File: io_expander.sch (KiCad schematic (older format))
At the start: 11 parts, among them IC1 MCP23008, P6 CONN_01X16, Q1 MTM232270LBF, Q2 MTM232270LBF, Q3 MTM232270LBF, Q4 MTM232270LBF, Q5 MTM232270LBF, Q6 MTM232270LBF, Q7 MTM232270LBF, Q8 MTM232270LBF

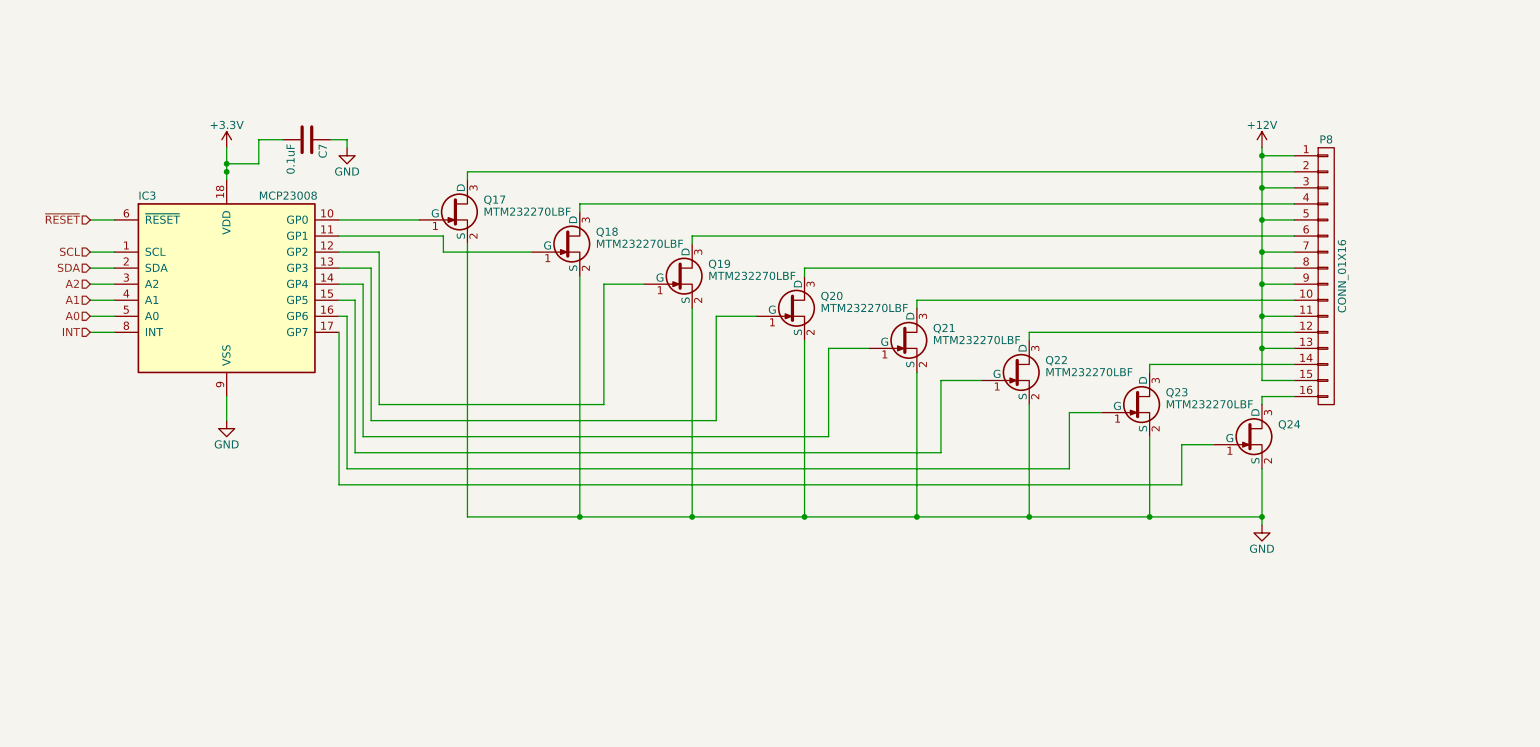
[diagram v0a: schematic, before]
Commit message: Rev B, Added Flywheel Diodes
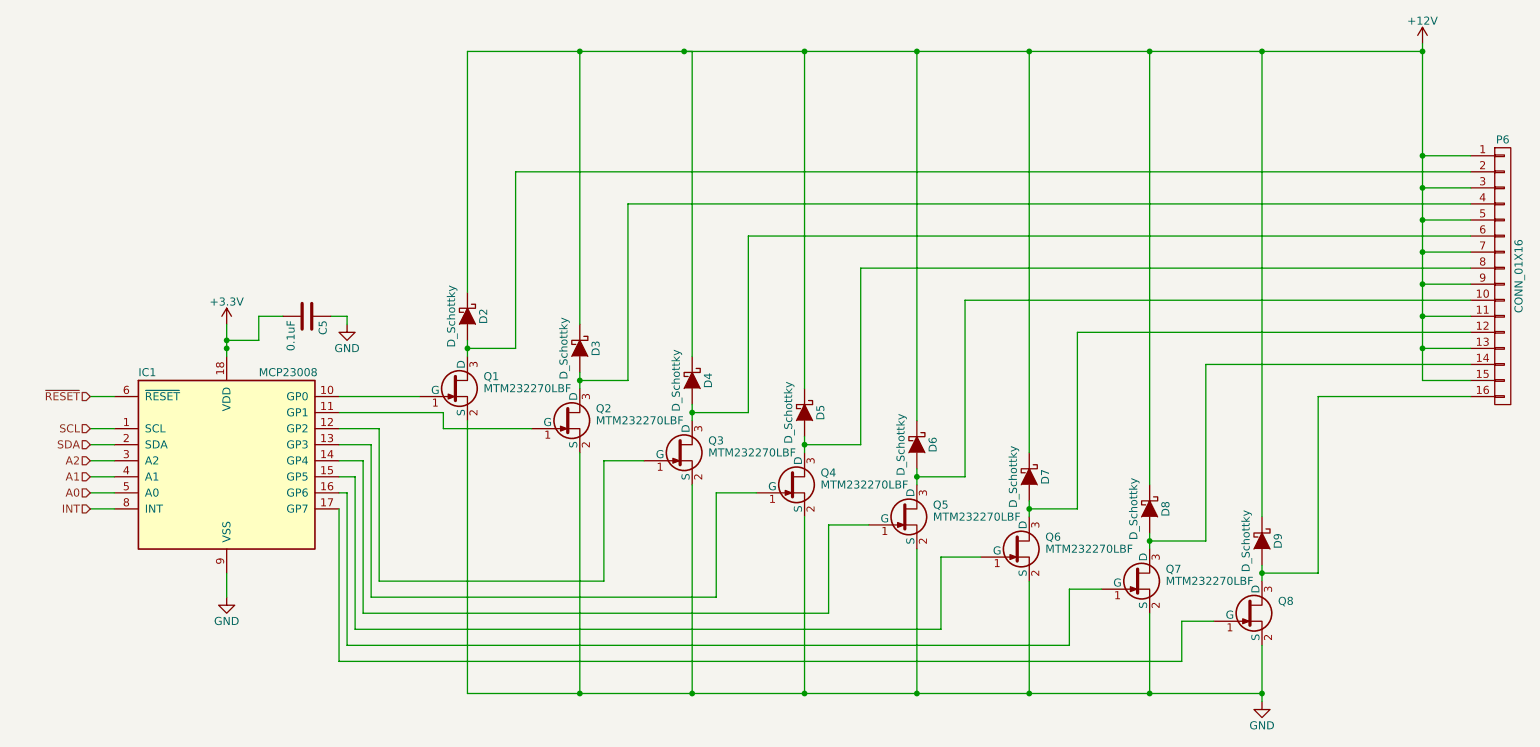
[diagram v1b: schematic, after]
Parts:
- added D17, D2, D3, D4, D5, D6, D7, D8: D_Schottky, Project Folder:microSMP, symbol D_Schottky
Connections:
- net +12V: now also D17.1 (K), D2.1 (K), D3.1 (K), D4.1 (K), D5.1 (K), D6.1 (K), D7.1 (K), D8.1 (K)
- net at P6.10 (P10), Q5.3 (D): now also D6.2 (A)
- net at P6.12 (P12), Q6.3 (D): now also D7.2 (A)
- net at P6.14 (P14), Q7.3 (D): now also D8.2 (A)
- net at P6.16 (P16), Q8.3 (D): now also D17.2 (A)
- net at P6.2 (P2), Q1.3 (D): now also D2.2 (A)
- net at P6.4 (P4), Q2.3 (D): now also D3.2 (A)
- net at P6.6 (P6), Q3.3 (D): now also D4.2 (A)
- net at P6.8 (P8), Q4.3 (D): now also D5.2 (A)
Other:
- moved on the sheet: C5, IC1, P6, Q1, Q2, Q3, Q4, Q5, Q6, Q7, Q8

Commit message: Added Fiducials and Fixed Diode Orientation
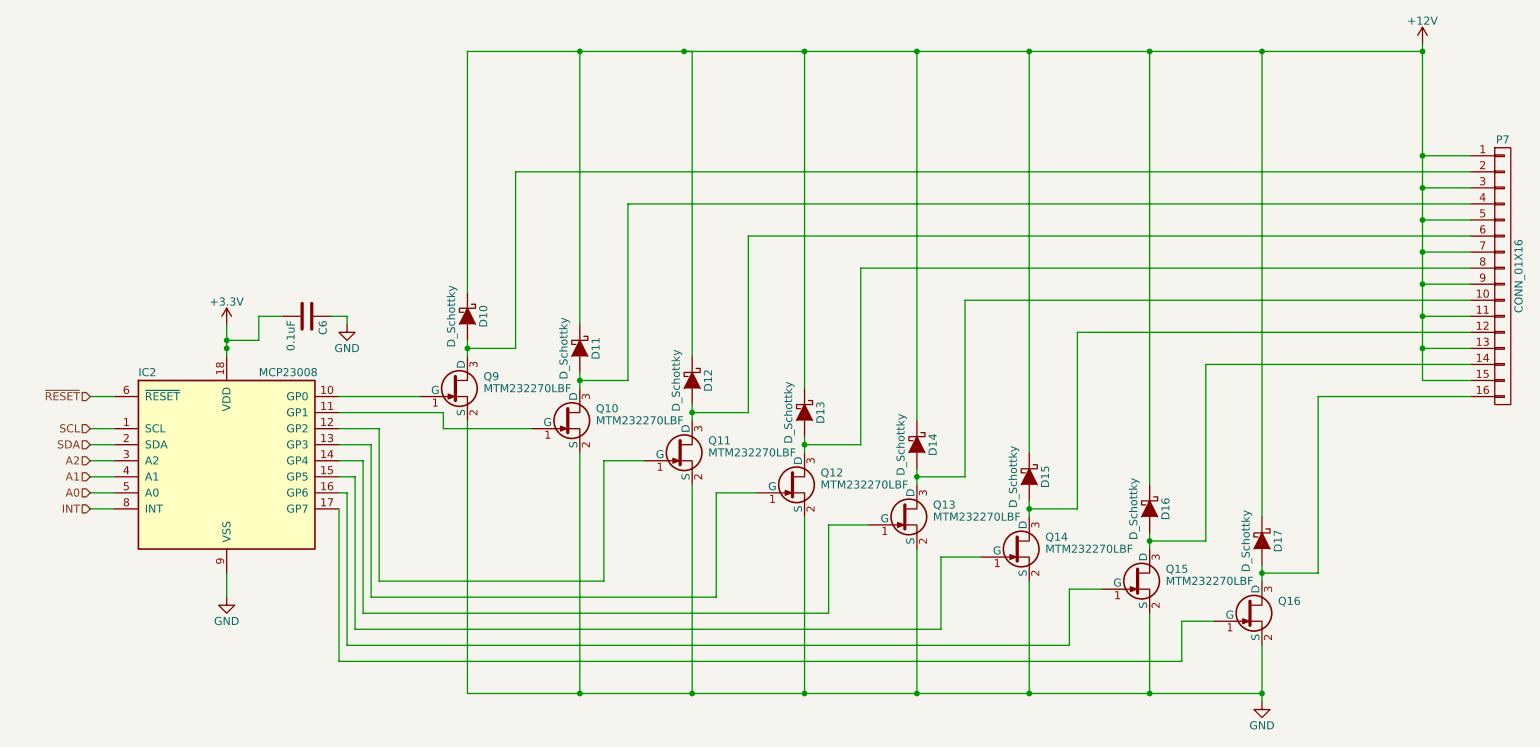
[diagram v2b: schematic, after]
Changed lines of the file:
@@
 $Descr A4 11693 8268
 encoding utf-8
-Sheet 2 5
+Sheet 3 5
 Title "The Open Bar Control Board"
-Date "2017-01-17"
-Rev "B"
+Date "2017-03-21"
+Rev "C"
 Comp "The Open Bar"
 Comment1 ""
@@
 AR Path="/56D78A1E/56D75806" Ref="P8"  Part="1"
 AR Path="/56D79252/56D75806" Ref="P9"  Part="1"
-F 0 "P6" H 11000 4400 50  0000 C CNN
+F 0 "P7" H 11000 4400 50  0000 C CNN
 F 1 "CONN_01X16" V 11100 3550 50  0000 C CNN
 F 2 "Terminal_Blocks:TerminalBlock_Pheonix_PT-3.5mm_16pol" H 11000 3550 50  0001 C CNN
@@
 AR Path="/56D78A1E/56D75807" Ref="Q17"  Part="1"
 AR Path="/56D79252/56D75807" Ref="Q25"  Part="1"
-F 0 "Q1" H 4650 4325 50  0000 L CNN
+F 0 "Q9" H 4650 4325 50  0000 L CNN
 F 1 "MTM232270LBF" H 4650 4250 50  0000 L CNN
 F 2 "TO_SOT_Packages_SMD:SC-70" H 4650 4175 50  0001 L CIN
@@
 AR Path="/56D78A1E/56D75808" Ref="Q18"  Part="1"
 AR Path="/56D79252/56D75808" Ref="Q26"  Part="1"
-F 0 "Q2" H 5350 4525 50  0000 L CNN
+F 0 "Q10" H 5350 4525 50  0000 L CNN
 F 1 "MTM232270LBF" H 5350 4450 50  0000 L CNN
 F 2 "TO_SOT_Packages_SMD:SC-70" H 5350 4375 50  0001 L CIN
@@
 AR Path="/56D78A1E/56D75809" Ref="Q19"  Part="1"
 AR Path="/56D79252/56D75809" Ref="Q27"  Part="1"
-F 0 "Q3" H 6050 4725 50  0000 L CNN
+F 0 "Q11" H 6050 4725 50  0000 L CNN
 F 1 "MTM232270LBF" H 6050 4650 50  0000 L CNN
 F 2 "TO_SOT_Packages_SMD:SC-70" H 6050 4575 50  0001 L CIN
@@
 AR Path="/56D78A1E/56D7580A" Ref="Q20"  Part="1"
 AR Path="/56D79252/56D7580A" Ref="Q28"  Part="1"
-F 0 "Q4" H 6750 4925 50  0000 L CNN
+F 0 "Q12" H 6750 4925 50  0000 L CNN
 F 1 "MTM232270LBF" H 6750 4850 50  0000 L CNN
 F 2 "TO_SOT_Packages_SMD:SC-70" H 6750 4775 50  0001 L CIN
@@
 AR Path="/56D78A1E/56D7580B" Ref="Q21"  Part="1"
 AR Path="/56D79252/56D7580B" Ref="Q29"  Part="1"
-F 0 "Q5" H 7450 5125 50  0000 L CNN
+F 0 "Q13" H 7450 5125 50  0000 L CNN
 F 1 "MTM232270LBF" H 7450 5050 50  0000 L CNN
 F 2 "TO_SOT_Packages_SMD:SC-70" H 7450 4975 50  0001 L CIN
@@
 AR Path="/56D78A1E/56D7580C" Ref="Q22"  Part="1"
 AR Path="/56D79252/56D7580C" Ref="Q30"  Part="1"
-F 0 "Q6" H 8150 5325 50  0000 L CNN
+F 0 "Q14" H 8150 5325 50  0000 L CNN
 F 1 "MTM232270LBF" H 8150 5250 50  0000 L CNN
 F 2 "TO_SOT_Packages_SMD:SC-70" H 8150 5175 50  0001 L CIN
@@
 AR Path="/56D78A1E/56D7580D" Ref="Q23"  Part="1"
 AR Path="/56D79252/56D7580D" Ref="Q31"  Part="1"
-F 0 "Q7" H 8900 5525 50  0000 L CNN
+F 0 "Q15" H 8900 5525 50  0000 L CNN
 F 1 "MTM232270LBF" H 8900 5450 50  0000 L CNN
 F 2 "TO_SOT_Packages_SMD:SC-70" H 8900 5375 50  0001 L CIN
@@
 AR Path="/56D78A1E/56D7580E" Ref="Q24"  Part="1"
 AR Path="/56D79252/56D7580E" Ref="Q32"  Part="1"
-F 0 "Q8" H 9600 5725 50  0000 L CNN
+F 0 "Q16" H 9600 5725 50  0000 L CNN
 F 1 "MTM232270LBF" H 9600 5650 50  0001 L CNN
 F 2 "TO_SOT_Packages_SMD:SC-70" H 9600 5575 50  0001 L CIN
@@
 AR Path="/56D78A1E/56D7580F" Ref="#PWR034"  Part="1"
 AR Path="/56D79252/56D7580F" Ref="#PWR039"  Part="1"
-F 0 "#PWR039" H 10500 1950 50  0001 C CNN
+F 0 "#PWR029" H 10500 1950 50  0001 C CNN
 F 1 "+12V" H 10500 2240 50  0000 C CNN
 F 2 "" H 10500 2100 50  0000 C CNN
@@
 AR Path="/56D78A1E/56D75818" Ref="#PWR035"  Part="1"
 AR Path="/56D79252/56D75818" Ref="#PWR040"  Part="1"
-F 0 "#PWR040" H 9500 5950 50  0001 C CNN
+F 0 "#PWR030" H 9500 5950 50  0001 C CNN
 F 1 "GND" H 9500 6050 50  0000 C CNN
 F 2 "" H 9500 6200 50  0000 C CNN
@@
 AR Path="/56D78A1E/56D75820" Ref="IC3"  Part="1"
 AR Path="/56D79252/56D75820" Ref="IC4"  Part="1"
-F 0 "IC1" H 2500 5250 50  0000 L CNN
+F 0 "IC2" H 2500 5250 50  0000 L CNN
 F 1 "MCP23008" H 3250 5250 50  0000 L CNN
 F 2 "Housings_SOIC:SOIC-18_7.5x11.6mm_Pitch1.27mm" H 3050 4700 50  0001 C CIN
@@
 AR Path="/56D78A1E/56D75821" Ref="#PWR036"  Part="1"
 AR Path="/56D79252/56D75821" Ref="#PWR041"  Part="1"
-F 0 "#PWR041" H 3050 5300 50  0001 C CNN
+F 0 "#PWR031" H 3050 5300 50  0001 C CNN
 F 1 "GND" H 3050 5400 50  0000 C CNN
 F 2 "" H 3050 5550 50  0000 C CNN
@@
 AR Path="/56D78A1E/56D75822" Ref="#PWR037"  Part="1"
 AR Path="/56D79252/56D75822" Ref="#PWR042"  Part="1"
-F 0 "#PWR042" H 3050 3700 50  0001 C CNN
+F 0 "#PWR032" H 3050 3700 50  0001 C CNN
 F 1 "+3.3V" H 3050 3990 50  0000 C CNN
 F 2 "" H 3050 3850 50  0000 C CNN
@@
 AR Path="/56D78A1E/56D75826" Ref="C7"  Part="1"
 AR Path="/56D79252/56D75826" Ref="C8"  Part="1"
-F 0 "C5" H 3575 3900 50  0000 L CNN
+F 0 "C6" H 3575 3900 50  0000 L CNN
 F 1 "0.1uF" H 3575 3700 50  0000 L CNN
 F 2 "Capacitors_SMD:C_0402" H 3588 3650 50  0001 C CNN
@@
 AR Path="/56D78A1E/56D75827" Ref="#PWR038"  Part="1"
 AR Path="/56D79252/56D75827" Ref="#PWR043"  Part="1"
-F 0 "#PWR043" H 3800 3600 50  0001 C CNN
+F 0 "#PWR033" H 3800 3600 50  0001 C CNN
 F 1 "GND" H 3800 3700 50  0000 C CNN
 F 2 "" H 3800 3850 50  0000 C CNN
@@
 AR Path="/56D78A1E/587E8B5C" Ref="D18"  Part="1"
 AR Path="/56D79252/587E8B5C" Ref="D26"  Part="1"
-F 0 "D2" H 4550 3900 50  0000 C CNN
+F 0 "D10" H 4550 3900 50  0000 C CNN
 F 1 "D_Schottky" H 4550 3700 50  0000 C CNN
 F 2 "Project Folder:microSMP" H 4550 3800 50  0001 C CNN
@@
 AR Path="/56D78A1E/587E90C4" Ref="D19"  Part="1"
 AR Path="/56D79252/587E90C4" Ref="D27"  Part="1"
-F 0 "D3" H 5250 4100 50  0000 C CNN
+F 0 "D11" H 5250 4100 50  0000 C CNN
 F 1 "D_Schottky" H 5250 3900 50  0000 C CNN
 F 2 "Project Folder:microSMP" H 5250 4000 50  0001 C CNN
@@
 AR Path="/56D78A1E/587E9153" Ref="D20"  Part="1"
 AR Path="/56D79252/587E9153" Ref="D28"  Part="1"
-F 0 "D4" H 5950 4300 50  0000 C CNN
+F 0 "D12" H 5950 4300 50  0000 C CNN
 F 1 "D_Schottky" H 5950 4100 50  0000 C CNN
 F 2 "Project Folder:microSMP" H 5950 4200 50  0001 C CNN
@@
 AR Path="/56D78A1E/587E91AD" Ref="D21"  Part="1"
 AR Path="/56D79252/587E91AD" Ref="D29"  Part="1"
-F 0 "D5" H 6650 4500 50  0000 C CNN
+F 0 "D13" H 6650 4500 50  0000 C CNN
 F 1 "D_Schottky" H 6650 4300 50  0000 C CNN
 F 2 "Project Folder:microSMP" H 6650 4400 50  0001 C CNN
@@
 AR Path="/56D78A1E/587E920E" Ref="D22"  Part="1"
 AR Path="/56D79252/587E920E" Ref="D30"  Part="1"
-F 0 "D6" H 7350 4700 50  0000 C CNN
+F 0 "D14" H 7350 4700 50  0000 C CNN
 F 1 "D_Schottky" H 7350 4500 50  0000 C CNN
 F 2 "Project Folder:microSMP" H 7350 4600 50  0001 C CNN
@@
 AR Path="/56D78A1E/587E926C" Ref="D23"  Part="1"
 AR Path="/56D79252/587E926C" Ref="D31"  Part="1"
-F 0 "D7" H 8050 4900 50  0000 C CNN
+F 0 "D15" H 8050 4900 50  0000 C CNN
 F 1 "D_Schottky" H 8050 4700 50  0000 C CNN
 F 2 "Project Folder:microSMP" H 8050 4800 50  0001 C CNN
@@
 AR Path="/56D78A1E/587E92CB" Ref="D24"  Part="1"
 AR Path="/56D79252/587E92CB" Ref="D32"  Part="1"
-F 0 "D8" H 8800 5100 50  0000 C CNN
+F 0 "D16" H 8800 5100 50  0000 C CNN
 F 1 "D_Schottky" H 8800 4900 50  0000 C CNN
 F 2 "Project Folder:microSMP" H 8800 5000 50  0001 C CNN
@@
 AR Path="/56D78A1E/587E9794" Ref="D25"  Part="1"
 AR Path="/56D79252/587E9794" Ref="D33"  Part="1"
-F 0 "D9" H 9500 5300 50  0000 C CNN
+F 0 "D17" H 9500 5300 50  0000 C CNN
 F 1 "D_Schottky" H 9500 5100 50  0000 C CNN
 F 2 "Project Folder:microSMP" H 9500 5200 50  0001 C CNN
